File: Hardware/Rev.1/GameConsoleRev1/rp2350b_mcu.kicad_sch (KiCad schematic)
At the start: 25 parts, among them J1 SWD-DAPLink, U1 RP2350B-QFN80, Y1 12MHz

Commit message: Added sprites
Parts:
- added C18, C25, C27: 100n, Capacitor_SMD:C_0402_1005Metric, symbol Device:C
- added C19, C29: 4u7, Capacitor_SMD:C_0402_1005Metric, symbol Device:C
- added C26, C28: 2u2, Capacitor_SMD:C_0402_1005Metric, symbol Device:C
- added R10, R8: 10k, Resistor_SMD:R_0805_2012Metric, symbol Device:R
- added R7, R9: 1k, Resistor_SMD:R_0805_2012Metric, symbol Device:R
- added SW1: NRST, Button_Switch_SMD:SW_Push_1P1T_NO_Vertical_Wuerth_434133025816, symbol Switch:SW_SPST
- added SW2: NRST, Button_Switch_THT:SW_Tactile_SPST_Angled_PTS645Vx58-2LFS, symbol Switch:SW_SPST
- added SW3: BOOTSEL, Button_Switch_SMD:SW_Push_1P1T_NO_Vertical_Wuerth_434133025816, symbol Switch:SW_SPST
- added U5: W25Q128JVS, Package_SO:SOIC-8_5.3x5.3mm_P1.27mm, symbol Memory_Flash:W25Q128JVS
- added U6: ESP-PSRAM64, Package_SO:SOIC-8_3.9x4.9mm_P1.27mm, symbol Memory_RAM:ESP-PSRAM32
- C1, C10, C11, C13, C2, C3, C4, C5, C6, C7, C8, C9: footprint (none) -> Capacitor_SMD:C_0402_1005Metric; LCSC (none) -> C307331
- C12: footprint (none) -> Capacitor_SMD:C_0402_1005Metric; LCSC (none) -> C23733
- C14, C15: footprint (none) -> Capacitor_SMD:C_0402_1005Metric; LCSC (none) -> C1548
- C16, C17: value 100n -> 4u7; footprint (none) -> Capacitor_SMD:C_0402_1005Metric; LCSC (none) -> C23733
- J1: footprint (none) -> Connector_PinHeader_2.54mm:PinHeader_1x03_P2.54mm_Vertical
- L1: footprint (none) -> REGI:AOTA-B201610S3R3-101-T; LCSC (none) -> C42411119; Name (none) -> AOTA-B201610S3R3-101-T
- R1, R2, R3: footprint (none) -> Capacitor_SMD:C_0402_1005Metric
- R4: value 27R -> 33R; footprint (none) -> Capacitor_SMD:C_0402_1005Metric
- U1: LCSC (none) -> C42415655
- Y1: value 12MHz -> ABM8-272-T3 [12MHz]; footprint (none) -> Crystal:Crystal_SMD_3225-4Pin_3.2x2.5mm; LCSC (none) -> C20625731
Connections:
- net +1V1: now also C18.1
- net +3V3: now also C19.1, C25.1, C26.1, C27.1, C28.1, C29.1, R10.1, R8.1, U5.8 (VCC), U6.8 (VCC)
- net GND: now also C18.2, C19.2, C25.2, C26.2, C27.2, C28.2, C29.2, R7.1, SW3.1 (A), U5.4 (GND), U6.4 (VSS)
- net QSPI_SCLK: now also U5.6 (CLK), U6.6 (SCLK)
- net QSPI_SD0: now also U5.5 (DI/IO_{0}), U6.5 (SI/SIO)
- net QSPI_SD1: now also U5.2 (DO/IO_{1}), U6.2 (SO/SIO)
- net QSPI_SD2: now also U5.3 (~{WP}/IO_{2}), U6.3 (SIO2)
- net QSPI_SD3: now also U5.7 (~{HOLD}/~{RESET}/IO_{3}), U6.7 (SIO3)
- net QSPI_SS: now also R10.2, R9.2, U5.1 (~{CS})
- net RUN: now also R8.2, SW1.2 (B), SW2.2 (B)
- net GPIO40_ADC0 renamed GPIO40
- net GPIO41_ADC1 renamed GPIO41
- net GPIO42_ADC2 renamed GPIO42
- net GPIO43_ADC3 renamed GPIO43
- net GPIO44_ADC4 renamed GPIO44
- net GPIO45_ADC5 renamed GPIO45
- net GPIO46_ADC6 renamed GPIO46
- net GPIO47_ADC7 renamed GPIO47
- net GPIO8 renamed GPIO8/PSRAM_CS
- net GPIO8/PSRAM_CS: now also U6.1 (~{CE})
- new net: R7.2, SW1.1 (A), SW2.1 (A)
- new net ~{USB_BOOT}: R9.1, SW3.2 (B)
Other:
- added sheet Peripherals (Peripherals.kicad_sch)
- note added: "128MBit/8Bits = 16MBytes"
- note added: "External Reset On the side of the box"
- moved on the sheet: C1, C10, C11, C12, C13, C14, C15, C16, C17, C2, C3, C4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

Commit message: A
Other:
- note added: "GPIO12"
- note added: "GPIO13"
- note added: "GPIO14"
- note added: "GPIO15"
- note added: "GPIO16"
- note added: "GPIO17"
- note added: "GPIO18"
- note added: "GPIO19"
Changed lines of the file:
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@@
 		)
 	)
+	(text "GPIO15"
+		(exclude_from_sim no)
+		(at 145.288 87.376 0)
+		(effects
+			(font
+				(size 1.27 1.27)
+			)
+			(justify left bottom)
+		)
+	)
+	(text "GPIO19"
+		(exclude_from_sim no)
+		(at 145.288 97.536 0)
+		(effects
+			(font
+				(size 1.27 1.27)
+			)
+			(justify left bottom)
+		)
+	)
+	(text "GPIO16"
+		(exclude_from_sim no)
+		(at 145.288 89.916 0)
+		(effects
+			(font
+				(size 1.27 1.27)
+			)
+			(justify left bottom)
+		)
+	)
+	(text "GPIO14"
+		(exclude_from_sim no)
+		(at 145.288 84.836 0)
+		(effects
+			(font
+				(size 1.27 1.27)
+			)
+			(justify left bottom)
+		)
+	)
+	(text "GPIO17"
+		(exclude_from_sim no)
+		(at 145.288 92.456 0)
+		(effects
+			(font
+				(size 1.27 1.27)
+			)
+			(justify left bottom)
+		)
+	)
 	(text "128MBit/8Bits = 16MBytes"
 		(exclude_from_sim no)
@@
 		)
 	)
+	(text "GPIO18"
+		(exclude_from_sim no)
+		(at 145.288 94.996 0)
+		(effects
+			(font
+				(size 1.27 1.27)
+			)
+			(justify left bottom)
+		)
+	)
 	(text "External Reset On the side of the box"
 		(exclude_from_sim no)
@@
 		)
 	)
+	(text "GPIO12"
+		(exclude_from_sim no)
+		(at 145.288 79.756 0)
+		(effects
+			(font
+				(size 1.27 1.27)
+			)
+			(justify left bottom)
+		)
+	)
+	(text "GPIO13"
+		(exclude_from_sim no)
+		(at 145.288 82.296 0)
+		(effects
+			(font
+				(size 1.27 1.27)
+			)
+			(justify left bottom)
+		)
+	)
 	(text_box "8SOIC 64MBit PSRAM"
 		(exclude_from_sim no)
@@
 			"YQB5AG8AdQB0ACgAKQAiACAAbABhAHkAbwB1AHQAcABvAHMAPQAiAHQAbwBwACIAIAAvAD4ADQAN"
 			"AAoAPAAvAGUAbABlAG0AZQBuAHQAPgANAA0ACgA8AGUAbABlAG0AZQBuAHQAIAByAGUAcwBpAGQA"
-			"PQAiAA=="
-		)
-	)
-	(label "GPIO18"
-		(at 124.46 95.25 0)
-		(effects
-			(font
-				(size 1.27 1.27)
-			)
-			(justify left bottom)
+			"PQAiAAAAAAAAAAAAAAAAAAAAAAAAAAAAAAAAAAAAAAAAAAAAAAAAAAAAAAAAAAAAAAAAAAAAAAAA"
+			"AAAAAAAAAAAAAAAAAAAAAAAAAAAAAAAAAAAAAAAAAAAAAAAAAAAAAAAAAAAAAAAAAAAAAAAAAAAA"
+			"AAAAAAAAAAAAAAAAAAAAAAAAAAAAAAAAAAAAAAAAAAAAAAAAAAAAAAAAAAAAAAAAAAAAAAAAAAAA"
+			"AAAAAAAAAAAAAAAAAAAAAAAAAAAAAAAAAAAAAAAAAAAAAAAAAAAAAAAAAAAAAAAAAAAAAAAAAAAA"
+			"AAAAAAAAAAAAAAAAAAAAAAAAAAAAAAAAAAAAAAAAAAAAAAAAAAAAAAAAAAAAAAAAAAAAAAAAAAAA"
+			"AAAAAAAAAAAAAAAAAAAAAAAAAAAAAAAAAAAAAAAAAAAAAAAAAAAAAAAAAAAAAAAAAAAAAAAAAAAA"
+			"AAAAAAAAAAAAAAAAAAAAAAAAAAAAAAAAAAAAAAAAAAAAAAAAAAAAAAAAAAAAAAAAAAAAAAAAAAAA"
+			"AAAAAAAAAAAAAAAAAAAAAAAAAAAAAAAAAAAAAAAAAAAAAAAAAAAAAAAAAAAAAAAAAAAAAAAAAAAA"
+			"AAAAAAAAAAAAAAAAAAAAAAAAAAAAAAAAAAAAAAAAAAAAAAAAAAAAAAAAAAAAAAAAAAAAAAAAAAAA"
+			"AAAAAAAAAAAAAAAAAAAAAAAAAAAAAAAAAAAAAAAAAAAAAAAAAAAAAAAAAAAAAAAAAAAAAAAAAAAA"
+			"AAAAAAAAAAAAAAAAAAAAAAAAAAAAAAAAAAAAAAAAAAAAAAAAAAAAAAAAAAAAAAAAAAAAAAAAAAAA"
+			"AAAAAAAAAAAAAAAAAAAAAAAAAAAAAAAAAAAAAAAAAAAAAAAAAAAAAAAAAAAAAAAAAAAAAAAAAAAA"
+			"AAAAAAAAAAAAAAAAAAAAAAAAAAAAAAAAAAAAAAAAAAAAAAAAAAAAAAAAAAAAAAAAAAAAAAAAAAAA"
+			"AAAAAAAAAAAAAAAAAAAAAAAAAAAAAAAAAAAAAAAAAAAAAAAAAAAAAAAAAAAAAAAAAAAAAAAAAAAA"
+			"AAAAAAAAAAAAAAAAAAAAAAAAAAAAAAAAAAAAAAAAAAAAAAAAAAAAAAAAAAAAAAAAAAAAAAAAAAAA"
+			"AAAAAAAAAAAAAAAAAAAAAAAAAAAAAAAAAAAAAAAAAAAAAAAAAAAAAAAAAAAAAAAAAAAAAAAAAAAA"
+			"AAAAAAAAAAAAAAAAAAAAAAAAAAAAAAAAAAAAAAAAAAAAAAAAAAAAAAAAAAAAAAAAAAAAAAAAAAAA"
+			"AAAAAAAAAAAAAAAAAAAAAAAAAAAAAAAAAAAAAAAAAAAAAAAAAAAAAAAAAAAAAAAAAAAAAAAAAAAA"
+			"AAAAAA=="
 		)
 	)
@@
 		)
 	)
-	(label "GPIO15"
-		(at 124.46 87.63 0)
-		(effects
-			(font
-				(size 1.27 1.27)
-			)
-			(justify left bottom)
-		)
-	)
 	(label "GPIO25"
 		(at 124.46 113.03 0)
@@
 		)
 	)
-	(label "GPIO19"
-		(at 124.46 97.79 0)
-		(effects
-			(font
-				(size 1.27 1.27)
-			)
-			(justify left bottom)
-		)
-	)
 	(label "SWDIO"
 		(at 273.05 31.75 180)
@@
 		)
 	)
-	(label "GPIO12"
-		(at 124.46 80.01 0)
-		(effects
-			(font
-				(size 1.27 1.27)
-			)
-			(justify left bottom)
-		)
-	)
 	(label "XIN"
 		(at 48.26 85.09 180)
@@
 		)
 	)
+	(label "GPIO17"
+		(at 124.46 92.71 0)
+		(effects
+			(font
+				(size 1.27 1.27)
+			)
+			(justify left bottom)
+		)
+	)
 	(label "QSPI_SS"
 		(at 237.49 133.35 180)
@@
 		)
 	)
+	(label "GPIO12"
+		(at 124.46 80.01 0)
+		(effects
+			(font
+				(size 1.27 1.27)
+			)
+			(justify left bottom)
+		)
+	)
 	(label "QSPI_SCLK"
 		(at 237.49 135.89 180)
@@
 		)
 	)
+	(label "GPIO19"
+		(at 124.46 97.79 0)
+		(effects
+			(font
+				(size 1.27 1.27)
+			)
+			(justify left bottom)
+		)
+	)
 	(label "XOUT"
 		(at 48.26 90.17 180)
@@
 		)
 	)
-	(label "GPIO17"
-		(at 124.46 92.71 0)
-		(effects
-			(font
-				(size 1.27 1.27)
-			)
-			(justify left bottom)
-		)
-	)
 	(label "GPIO35"
 		(at 124.46 138.43 0)
@@
 		)
 	)
-	(label "GPIO0"
-		(at 124.46 49.53 0)
+	(label "GPIO16"
+		(at 124.46 90.17 0)
 		(effects
 			(font
@@
 		)
 	)
-	(label "GPIO8{slash}PSRAM_CS"
-		(at 265.43 92.71 0)
+	(label "GPIO0"
+		(at 124.46 49.53 0)
 		(effects
 			(font
@@
 		)
 	)
-	(label "GPIO16"
-		(at 124.46 90.17 0)
+	(label "GPIO8{slash}PSRAM_CS"
+		(at 265.43 92.71 0)
 		(effects
 			(font
@@
 		)
 	)
+	(label "GPIO18"
+		(at 124.46 95.25 0)
+		(effects
+			(font
+				(size 1.27 1.27)
+			)
+			(justify left bottom)
+		)
+	)
 	(label "GPIO20"
 		(at 124.46 100.33 0)
@@
 		)
 	)
+	(label "GPIO14"
+		(at 124.46 85.09 0)
+		(effects
+			(font
+				(size 1.27 1.27)
+			)
+			(justify left bottom)
+		)
+	)
 	(label "GPIO45"
 		(at 124.46 166.37 0)
@@
 		)
 	)
-	(label "GPIO14"
-		(at 124.46 85.09 0)
+	(label "GPIO8{slash}PSRAM_CS"
+		(at 124.46 69.85 0)
 		(effects
 			(font
@@
 		)
 	)
-	(label "GPIO8{slash}PSRAM_CS"
-		(at 124.46 69.85 0)
+	(label "XOUT"
+		(at 156.21 91.44 180)
 		(effects
 			(font
 				(size 1.27 1.27)
 			)
-			(justify left bottom)
+			(justify right bottom)
 		)
 	)
-	(label "XOUT"
-		(at 156.21 91.44 180)
+	(label "GPIO15"
+		(at 124.46 87.63 0)
 		(effects
 			(font
 				(size 1.27 1.27)
 			)
-			(justify right bottom)
+			(justify left bottom)
 		)
 	)
@@
 		)
 	)
+	(label "GPIO13"
+		(at 124.46 82.55 0)
+		(effects
+			(font
+				(size 1.27 1.27)
+			)
+			(justify left bottom)
+		)
+	)
 	(label "GPIO42"
 		(at 124.46 158.75 0)
@@
 		)
 	)
-	(label "GPIO13"
-		(at 124.46 82.55 0)
-		(effects
-			(font
-				(size 1.27 1.27)
-			)
-			(justify left bottom)
-		)
-	)

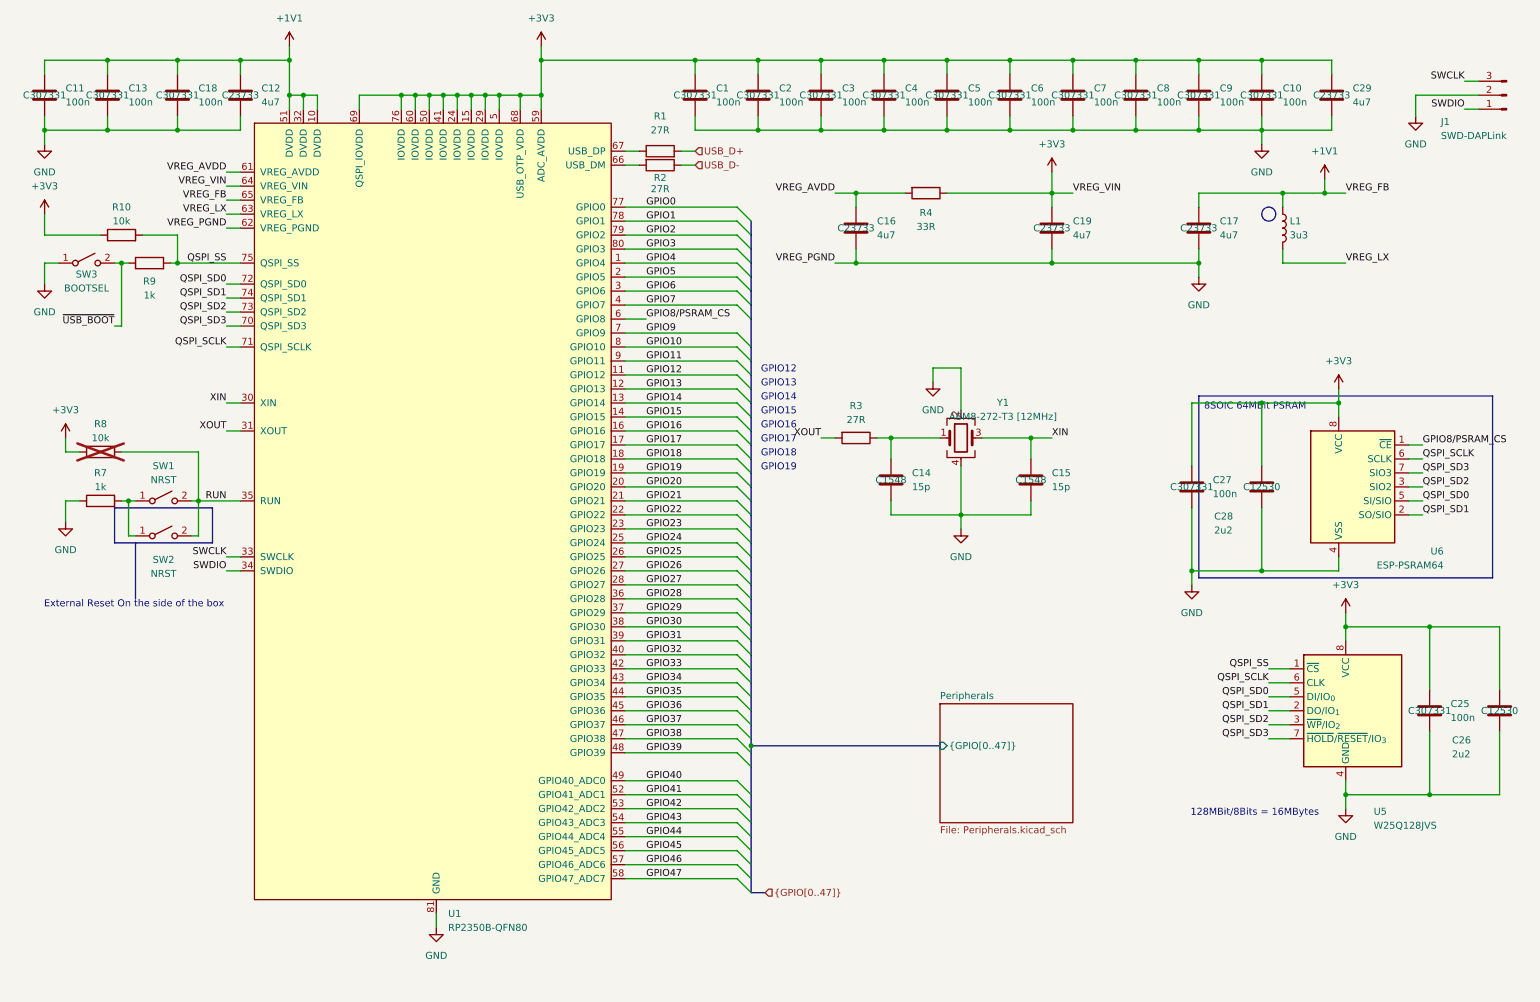
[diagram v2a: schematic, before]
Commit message: Added CPP Build
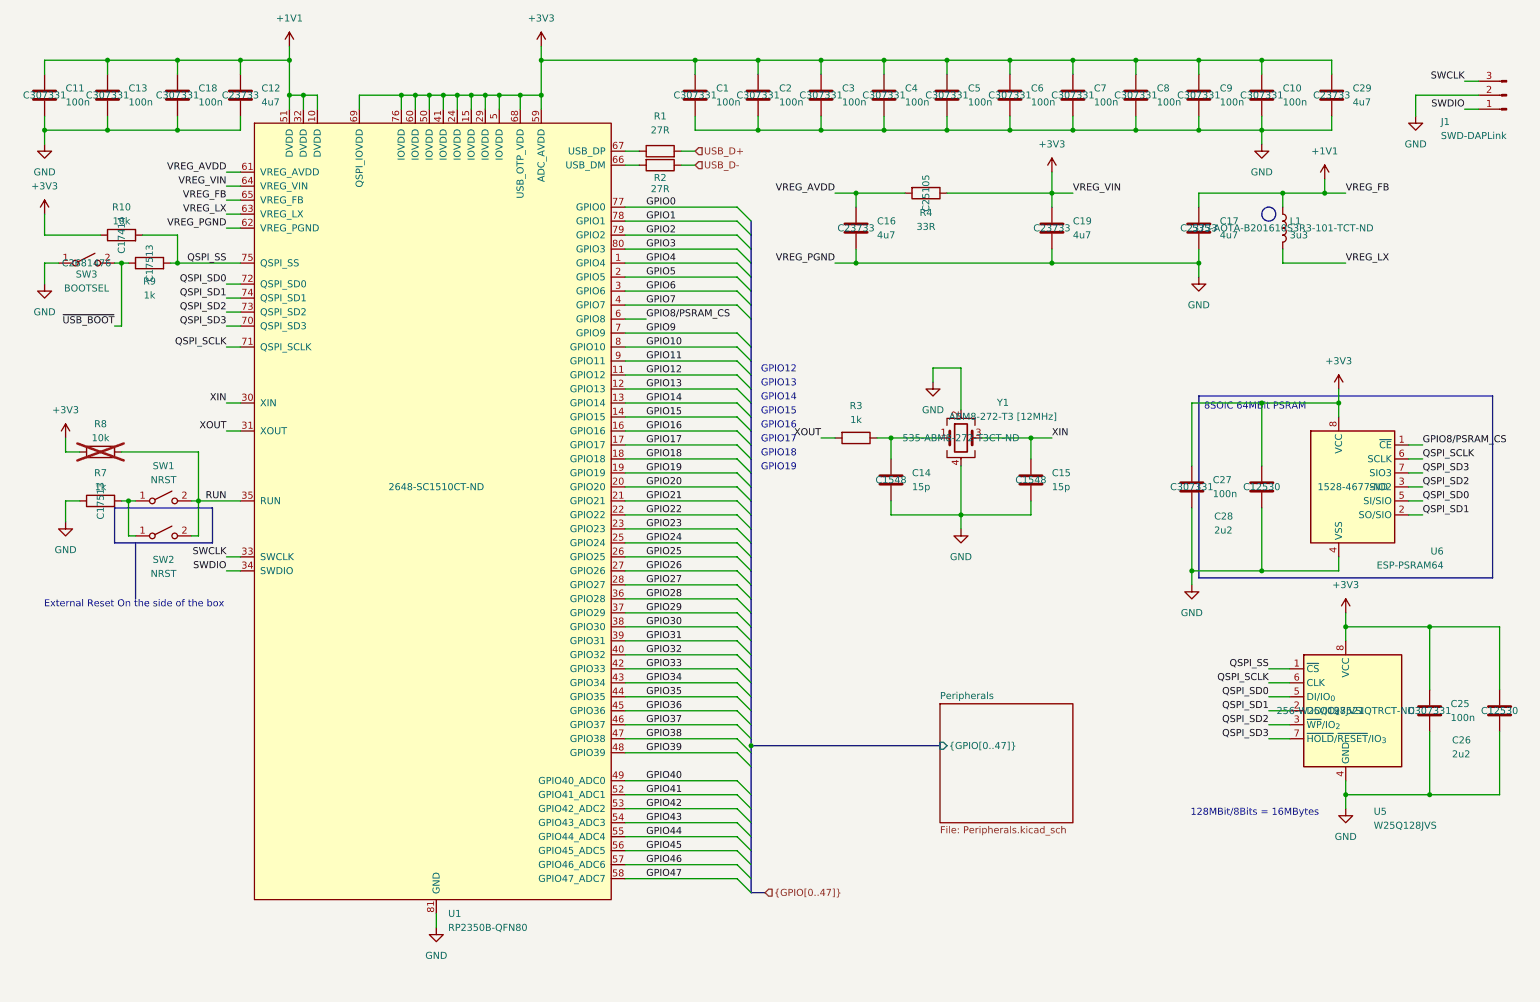
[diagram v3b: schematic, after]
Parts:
- L1: DK# (none) -> 535-AOTA-B201610S3R3-101-TCT-ND
- R1, R2: footprint Capacitor_SMD:C_0402_1005Metric -> Resistor_SMD:R_0603_1608Metric
- R10: LCSC (none) -> C17414
- R3: value 27R -> 1k; footprint Capacitor_SMD:C_0402_1005Metric -> Resistor_SMD:R_0402_1005Metric; LCSC (none) -> C11702
- R4: footprint Capacitor_SMD:C_0402_1005Metric -> Resistor_SMD:R_0402_1005Metric; LCSC (none) -> C25105
- R7, R9: LCSC (none) -> C17513
- SW1, SW3: LCSC (none) -> C2681476
- U1: DK# (none) -> 2648-SC1510CT-ND
- U5: DK# (none) -> 256-W25Q128JVSIQTRCT-ND; LCSC (none) -> C97521
- U6: DK# (none) -> 1528-4677-ND
- Y1: DK# (none) -> 535-ABM8-272-T3CT-ND
